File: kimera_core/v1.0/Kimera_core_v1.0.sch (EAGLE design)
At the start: 15 parts, among them IC1 PCA9555RGER, IC2 PCA9555RGER, Q1 CSTCR6M00G53Z, U1 ATMEGA32U4QFN

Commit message: kimera_core: Change bus and layout
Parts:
- added JP1, JP2, JP3, JP4: (no value), castellation:P12
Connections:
- net N$1 renamed RESET
- net N$11 renamed SDA
- removed net N$10: IC1.SCL, R5.1, U1.PD0(SCL)
- new net A1: IC1.A1, IC2.A1
- new net A2: IC1.A2, IC2.A2
- new net MISO: U1.PB3(MISO)
- new net MOSI: U1.PB2(MOSI)
- new net P1: IC1.P00, JP2.7
- new net P10: IC1.P11, JP1.4
- new net P11: IC1.P12, JP1.5
- new net P12: IC1.P13, JP1.6
- new net P13: IC1.P14, JP1.7
- new net P14: IC1.P15, JP1.8
- new net P15: IC1.P16, JP1.9
- new net P16: IC1.P17, JP1.10
- new net P17: IC2.P00, JP3.3
- new net P18: IC2.P01, JP3.4
- new net P19: IC2.P02, JP3.5
- new net P2: IC1.P01, JP2.8
- new net P20: IC2.P03, JP3.6
- new net P21: IC2.P04, JP3.7
- new net P22: IC2.P05, JP3.8
- new net P23: IC2.P06, JP3.9
- new net P24: IC2.P07, JP3.10
- new net P25: IC2.P10, JP3.11
- new net P26: IC2.P11, JP3.12
- new net P27: IC2.P12, JP2.1
- new net P28: IC2.P13, JP2.2
- new net P29: IC2.P14, JP2.3
- new net P3: IC1.P02, JP2.9
- new net P30: IC2.P15, JP2.4
- new net P31: IC2.P16, JP2.5
- new net P32: IC2.P17, JP2.6
- new net P4: IC1.P03, JP2.10
- new net P5: IC1.P04, JP2.11
- new net P6: IC1.P05, JP2.12
- new net P7: IC1.P06, JP1.1
- new net P8: IC1.P07, JP1.2
- new net P9: IC1.P10, JP1.3
- new net RX: U1.PD2(RX)
- new net SCK: U1.PB1(SCK)
- new net SCL: IC1.SCL, IC2.SCL, R5.1, U1.PD0(SCL)
- new net TX: U1.PD3(TX)
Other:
- moved on the sheet: C1, C2, C3, C4, C5, IC1, IC2, Q1, R1, R2, R3, R4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

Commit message: kimera_core: Change basic layout and route a part of io
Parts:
- added JP5, JP6: (no value), castellation:P08
- JP1, JP2, JP3, JP4: device castellation:P12 -> castellation:P08
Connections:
- net P1: now also JP1.1; no longer JP2.7
- net P10: now also JP2.2; no longer JP1.4
- net P11: now also JP2.3; no longer JP1.5
- net P12: now also JP2.4; no longer JP1.6
- net P13: now also JP2.5; no longer JP1.7
- net P14: now also JP2.6; no longer JP1.8
- net P15: now also JP2.7; no longer JP1.9
- net P16: now also JP2.8; no longer JP1.10
- net P17: now also JP3.1; no longer JP3.3
- net P18: now also JP3.2; no longer JP3.4
- net P19: now also JP3.3; no longer JP3.5
- net P2: now also JP1.2; no longer JP2.8
- net P20: now also JP3.4; no longer JP3.6
- net P21: now also JP3.5; no longer JP3.7
- net P22: now also JP3.6; no longer JP3.8
- net P23: now also JP3.7; no longer JP3.9
- net P24: now also JP3.8; no longer JP3.10
- net P25: now also JP4.1; no longer JP3.11
- net P26: now also JP4.2; no longer JP3.12
- net P27: now also JP4.3; no longer JP2.1
- net P28: now also JP4.4; no longer JP2.2
- net P29: now also JP4.5; no longer JP2.3
- net P3: now also JP1.3; no longer JP2.9
- net P30: now also JP4.6; no longer JP2.4
- net P31: now also JP4.7; no longer JP2.5
- net P32: now also JP4.8; no longer JP2.6
- net P4: now also JP1.4; no longer JP2.10
- net P5: now also JP1.5; no longer JP2.11
- net P6: now also JP1.6; no longer JP2.12
- net P7: now also JP1.7; no longer JP1.1
- net P8: now also JP1.8; no longer JP1.2
- net P9: now also JP2.1; no longer JP1.3
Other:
- moved on the sheet: R6

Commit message: kimera_core: Assign main io and route more io
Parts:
- JP5, JP6: device castellation:P08 -> castellation:P10
- U1: value ATMEGA32U4QFN -> ATMEGA32U4QFN2; device SparkFun-DigitalIC:ATMEGA32U4QFN -> SparkFun-DigitalIC:ATMEGA32U4QFN2
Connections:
- removed net N$8: R2.1
- removed net N$9: R3.1
- new net D+: JP5.3, R2.1
- new net D-: JP5.2, R3.1
- new net N$10: JP6.4
- new net N$11: JP6.5
- new net N$13: JP6.6
- new net N$14: JP6.7
- new net N$15: JP6.8
- new net N$16: JP6.9
- new net N$17: JP6.10
- net 5V: now also JP5.1, JP6.1
- net GND: now also JP5.4
- net MISO: now also JP5.7
- net MOSI: now also JP5.6
- net RESET: now also JP5.8
- net RX: now also JP6.3
- net SCK: now also JP5.5
- net SCL: now also JP5.9
- net SDA: now also JP5.10
- net TX: now also JP6.2
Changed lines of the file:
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@@
 </classes>
 <parts>
-<part name="U1" library="SparkFun-DigitalIC" deviceset="ATMEGA32U4" device="QFN"/>
+<part name="U1" library="SparkFun-DigitalIC" deviceset="ATMEGA32U4" device="QFN2" value="ATMEGA32U4QFN2"/>
 <part name="FRAME1" library="SparkFun-Aesthetics" deviceset="FRAME-A4L" device="">
 <attribute name="CNAME" value="Noukensha"/>
@@
 <part name="JP3" library="castellation" deviceset="P08" device=""/>
 <part name="JP4" library="castellation" deviceset="P08" device=""/>
-<part name="JP5" library="castellation" deviceset="P08" device=""/>
-<part name="JP6" library="castellation" deviceset="P08" device=""/>
+<part name="JP5" library="castellation" deviceset="P10" device=""/>
+<part name="JP6" library="castellation" deviceset="P10" device=""/>
 </parts>
 <sheets>
@@
 <instance part="R6" gate="G$1" x="129.54" y="149.86" rot="R90"/>
 <instance part="SUPPLY7" gate="G$1" x="129.54" y="157.48"/>
-<instance part="JP1" gate="G$1" x="129.54" y="50.8"/>
-<instance part="JP2" gate="G$1" x="147.32" y="50.8"/>
-<instance part="JP3" gate="G$1" x="165.1" y="50.8"/>
-<instance part="JP4" gate="G$1" x="182.88" y="50.8"/>
-<instance part="JP5" gate="G$1" x="200.66" y="50.8"/>
+<instance part="JP1" gate="G$1" x="124.46" y="53.34"/>
+<instance part="JP2" gate="G$1" x="142.24" y="53.34"/>
+<instance part="JP3" gate="G$1" x="160.02" y="53.34"/>
+<instance part="JP4" gate="G$1" x="177.8" y="53.34"/>
+<instance part="JP5" gate="G$1" x="195.58" y="50.8"/>
 <instance part="JP6" gate="G$1" x="218.44" y="50.8"/>
 </instances>
@@
 <wire x1="60.96" y1="142.24" x2="58.42" y2="142.24" width="0.1524" layer="91"/>
 <label x="58.42" y="142.24" size="1.27" layer="95" rot="R180" xref="yes"/>
+<junction x="60.96" y="142.24"/>
+</segment>
+<segment>
+<pinref part="JP5" gate="G$1" pin="8"/>
+<wire x1="205.74" y1="55.88" x2="208.28" y2="55.88" width="0.1524" layer="91"/>
+<label x="208.28" y="55.88" size="1.27" layer="95" xref="yes"/>
 </segment>
 </net>
@@
 <pinref part="SUPPLY7" gate="G$1" pin="5V"/>
 <wire x1="129.54" y1="154.94" x2="129.54" y2="157.48" width="0.1524" layer="91"/>
+</segment>
+<segment>
+<pinref part="JP5" gate="G$1" pin="1"/>
+<wire x1="205.74" y1="38.1" x2="208.28" y2="38.1" width="0.1524" layer="91"/>
+<label x="208.28" y="38.1" size="1.27" layer="95" xref="yes"/>
+</segment>
+<segment>
+<pinref part="JP6" gate="G$1" pin="1"/>
+<wire x1="228.6" y1="38.1" x2="231.14" y2="38.1" width="0.1524" layer="91"/>
+<label x="231.14" y="38.1" size="1.27" layer="95" xref="yes"/>
 </segment>
 </net>
@@
 <junction x="195.58" y="78.74"/>
 </segment>
+<segment>
+<pinref part="JP5" gate="G$1" pin="4"/>
+<wire x1="205.74" y1="45.72" x2="208.28" y2="45.72" width="0.1524" layer="91"/>
+<label x="208.28" y="45.72" size="1.27" layer="95" xref="yes"/>
+</segment>
 </net>
 <net name="N$3" class="0">
@@
 </segment>
 </net>
-<net name="N$8" class="0">
+<net name="D+" class="0">
 <segment>
 <pinref part="R2" gate="G$1" pin="1"/>
 <wire x1="40.64" y1="109.22" x2="38.1" y2="109.22" width="0.1524" layer="91"/>
-</segment>
-</net>
-<net name="N$9" class="0">
+<label x="38.1" y="109.22" size="1.27" layer="95" rot="R180" xref="yes"/>
+</segment>
+<segment>
+<pinref part="JP5" gate="G$1" pin="3"/>
+<wire x1="205.74" y1="43.18" x2="208.28" y2="43.18" width="0.1524" layer="91"/>
+<label x="208.28" y="43.18" size="1.27" layer="95" xref="yes"/>
+</segment>
+</net>
+<net name="D-" class="0">
 <segment>
 <pinref part="R3" gate="G$1" pin="1"/>
 <wire x1="43.18" y1="106.68" x2="38.1" y2="106.68" width="0.1524" layer="91"/>
+<label x="38.1" y="106.68" size="1.27" layer="95" rot="R180" xref="yes"/>
+</segment>
+<segment>
+<pinref part="JP5" gate="G$1" pin="2"/>
+<wire x1="205.74" y1="40.64" x2="208.28" y2="40.64" width="0.1524" layer="91"/>
+<label x="208.28" y="40.64" size="1.27" layer="95" xref="yes"/>
 </segment>
 </net>
@@
 <wire x1="129.54" y1="137.16" x2="129.54" y2="111.76" width="0.1524" layer="91"/>
 <junction x="129.54" y="111.76"/>
+</segment>
+<segment>
+<pinref part="JP5" gate="G$1" pin="9"/>
+<wire x1="205.74" y1="58.42" x2="208.28" y2="58.42" width="0.1524" layer="91"/>
+<label x="208.28" y="58.42" size="1.27" layer="95" xref="yes"/>
 </segment>
 </net>
@@
 <label x="114.3" y="109.22" size="1.27" layer="95" xref="yes"/>
 </segment>
+<segment>
+<pinref part="JP5" gate="G$1" pin="10"/>
+<wire x1="205.74" y1="60.96" x2="208.28" y2="60.96" width="0.1524" layer="91"/>
+<label x="208.28" y="60.96" size="1.27" layer="95" xref="yes"/>
+</segment>
 </net>
 <net name="N$12" class="0">
@@
 <label x="106.68" y="119.38" size="1.27" layer="95" xref="yes"/>
 </segment>
+<segment>
+<pinref part="JP6" gate="G$1" pin="3"/>
+<wire x1="228.6" y1="43.18" x2="231.14" y2="43.18" width="0.1524" layer="91"/>
+<label x="231.14" y="43.18" size="1.27" layer="95" xref="yes"/>
+</segment>
 </net>
 <net name="TX" class="0">
@@
 <label x="106.68" y="116.84" size="1.27" layer="95" xref="yes"/>
 </segment>
+<segment>
+<pinref part="JP6" gate="G$1" pin="2"/>
+<wire x1="228.6" y1="40.64" x2="231.14" y2="40.64" width="0.1524" layer="91"/>
+<label x="231.14" y="40.64" size="1.27" layer="95" xref="yes"/>
+</segment>
 </net>
 <net name="MISO" class="0">
@@
 <label x="106.68" y="76.2" size="1.27" layer="95" xref="yes"/>
 </segment>
+<segment>
+<pinref part="JP5" gate="G$1" pin="7"/>
+<wire x1="205.74" y1="53.34" x2="208.28" y2="53.34" width="0.1524" layer="91"/>
+<label x="208.28" y="53.34" size="1.27" layer="95" xref="yes"/>
+</segment>
 </net>
 <net name="MOSI" class="0">
@@
 <label x="106.68" y="78.74" size="1.27" layer="95" xref="yes"/>
 </segment>
+<segment>
+<pinref part="JP5" gate="G$1" pin="6"/>
+<wire x1="205.74" y1="50.8" x2="208.28" y2="50.8" width="0.1524" layer="91"/>
+<label x="208.28" y="50.8" size="1.27" layer="95" xref="yes"/>
+</segment>
 </net>
 <net name="SCK" class="0">
@@
 <label x="106.68" y="81.28" size="1.27" layer="95" xref="yes"/>
 </segment>
+<segment>
+<pinref part="JP5" gate="G$1" pin="5"/>
+<wire x1="205.74" y1="48.26" x2="208.28" y2="48.26" width="0.1524" layer="91"/>
+<label x="208.28" y="48.26" size="1.27" layer="95" xref="yes"/>
+</segment>
 </net>
 <net name="A1" class="0">
@@
 </segment>
 </net>
+<net name="N$10" class="0">
+<segment>
+<pinref part="JP6" gate="G$1" pin="4"/>
+<wire x1="228.6" y1="45.72" x2="231.14" y2="45.72" width="0.1524" layer="91"/>
+</segment>
+</net>
+<net name="N$11" class="0">
+<segment>
+<pinref part="JP6" gate="G$1" pin="5"/>
+<wire x1="228.6" y1="48.26" x2="231.14" y2="48.26" width="0.1524" layer="91"/>
+</segment>
+</net>
+<net name="N$13" class="0">
+<segment>
+<pinref part="JP6" gate="G$1" pin="6"/>
+<wire x1="228.6" y1="50.8" x2="231.14" y2="50.8" width="0.1524" layer="91"/>
+</segment>
+</net>
+<net name="N$14" class="0">
+<segment>
+<pinref part="JP6" gate="G$1" pin="7"/>
+<wire x1="228.6" y1="53.34" x2="231.14" y2="53.34" width="0.1524" layer="91"/>
+</segment>
+</net>
+<net name="N$15" class="0">
+<segment>
+<pinref part="JP6" gate="G$1" pin="8"/>
+<wire x1="228.6" y1="55.88" x2="231.14" y2="55.88" width="0.1524" layer="91"/>
+</segment>
+</net>
+<net name="N$16" class="0">
+<segment>
+<pinref part="JP6" gate="G$1" pin="9"/>
+<wire x1="228.6" y1="58.42" x2="231.14" y2="58.42" width="0.1524" layer="91"/>
+</segment>
+</net>
+<net name="N$17" class="0">
+<segment>
+<pinref part="JP6" gate="G$1" pin="10"/>
+<wire x1="228.6" y1="60.96" x2="231.14" y2="60.96" width="0.1524" layer="91"/>
+</segment>
+</net>

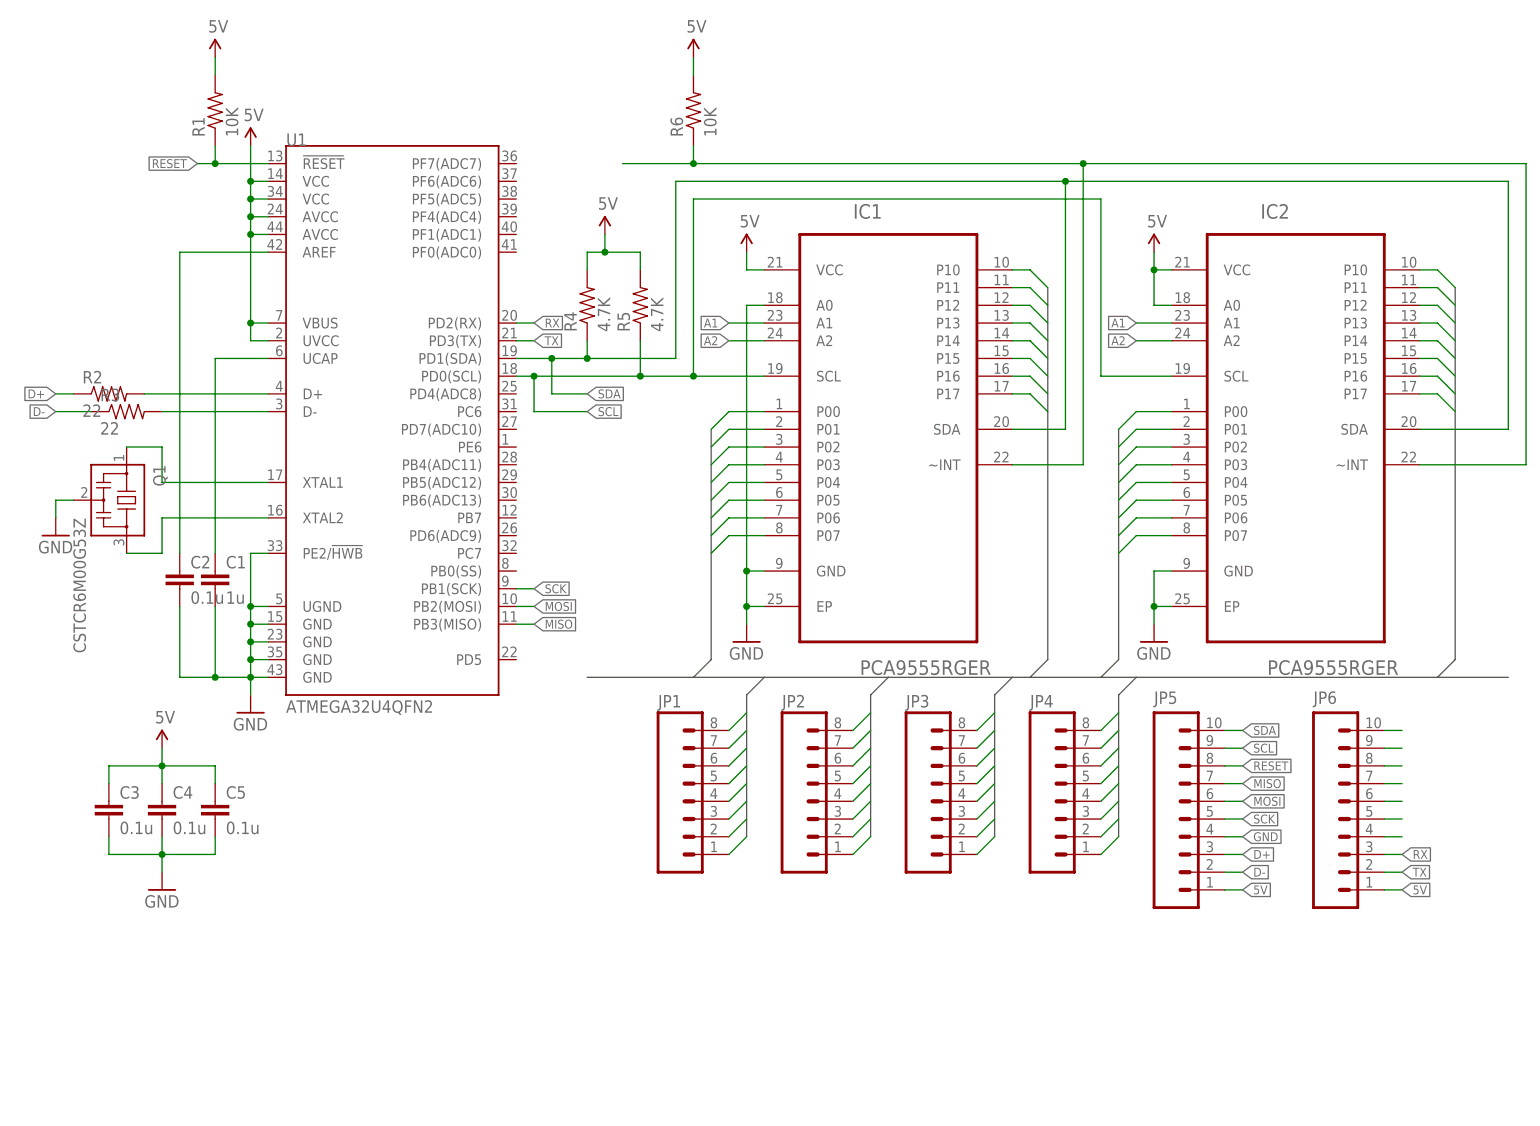
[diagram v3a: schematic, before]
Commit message: kimera_core: Change element location and castellated holes
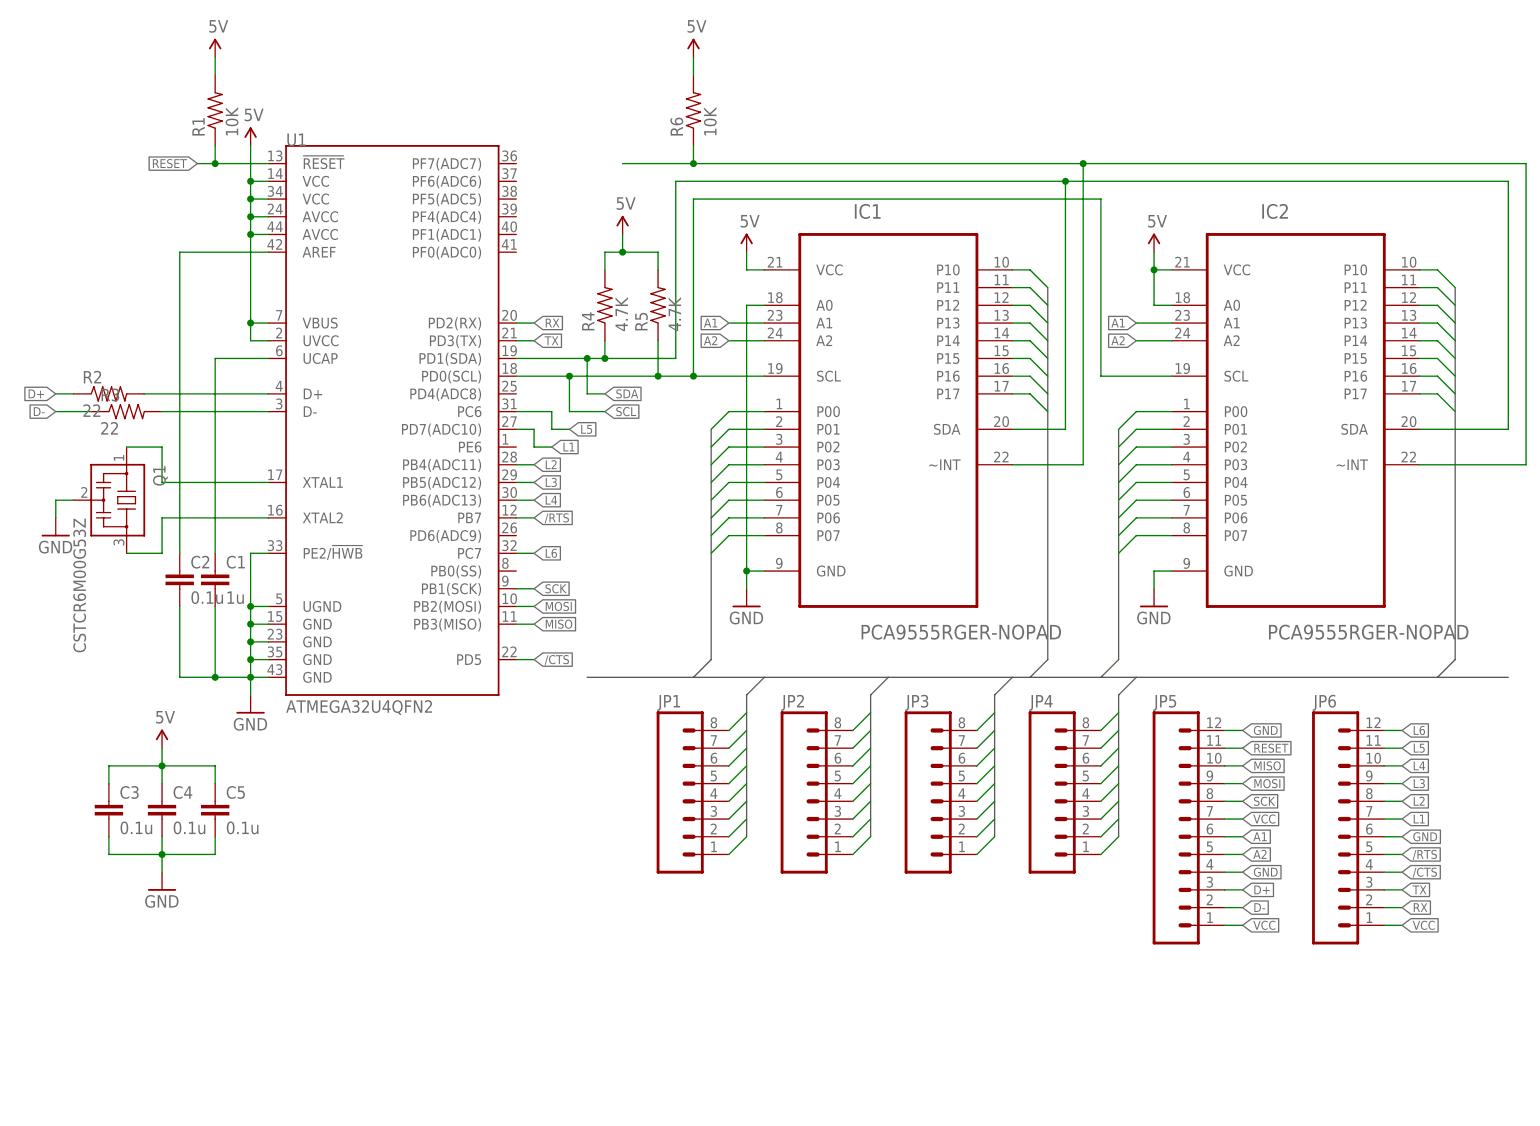
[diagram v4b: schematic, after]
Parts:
- IC1, IC2: value PCA9555RGER -> PCA9555RGER-NOPAD; device Texas Instruments_By_element14_Batch_1:PCA9555RGER -> pca9555:PCA9555RGER-NOPAD
- JP5, JP6: device castellation:P10 -> castellation:P12
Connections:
- removed net 5V: C3.1, C4.1, C5.1, IC1.VCC, IC2.A0, IC2.VCC, JP5.1, JP6.1, R1.2, R4.2, R5.2, R6.2, U1.AVCC@24, U1.AVCC@44, U1.UVCC, U1.VBUS, U1.VCC@14, U1.VCC@34
- removed net N$10: JP6.4
- removed net N$11: JP6.5
- removed net N$13: JP6.6
- removed net N$14: JP6.7
- removed net N$15: JP6.8
- removed net N$16: JP6.9
- removed net N$17: JP6.10
- new net /CTS: JP6.4, U1.PD5
- new net /RTS: JP6.5, U1.PB7
- new net L1: JP6.7, U1.PD7(ADC10)
- new net L2: JP6.8, U1.PB4(ADC11)
- new net L3: JP6.9, U1.PB5(ADC12)
- new net L4: JP6.10, U1.PB6(ADC13)
- new net L5: JP6.11, U1.PC6
- new net L6: JP6.12, U1.PC7
- new net VCC: C3.1, C4.1, C5.1, IC1.VCC, IC2.A0, IC2.VCC, JP5.1, JP5.7, JP6.1, R1.2, R4.2, R5.2, R6.2, U1.AVCC@24, U1.AVCC@44, U1.UVCC, U1.VBUS, U1.VCC@14, U1.VCC@34
- net A1: now also JP5.6
- net A2: now also JP5.5
- net GND: now also JP5.12, JP6.6; no longer IC1.EP, IC2.EP
- net MISO: now also JP5.10; no longer JP5.7
- net MOSI: now also JP5.9; no longer JP5.6
- net RESET: now also JP5.11; no longer JP5.8
- net RX: now also JP6.2; no longer JP6.3
- net SCK: now also JP5.8; no longer JP5.5
- net SCL: no longer JP5.9
- net SDA: no longer JP5.10
- net TX: now also JP6.3; no longer JP6.2
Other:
- moved on the sheet: R4, R5
